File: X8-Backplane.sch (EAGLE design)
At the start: 17 parts, among them IC1 MAX3467CPA, U1 LM2678

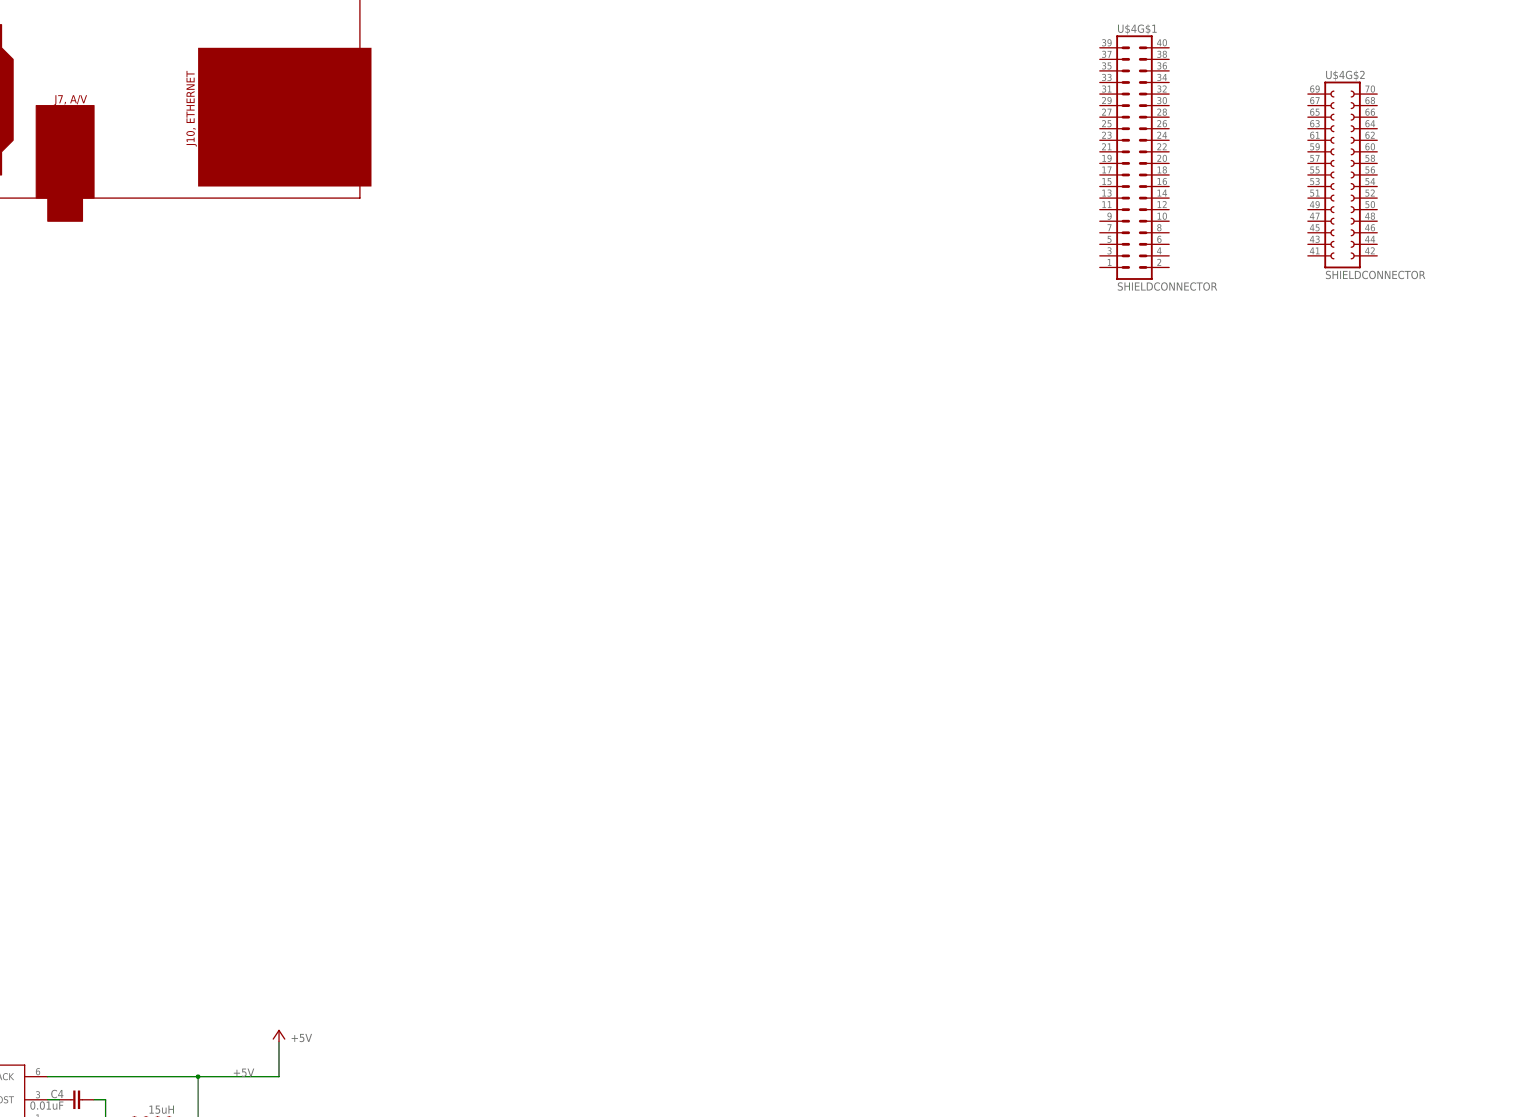
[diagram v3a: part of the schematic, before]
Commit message: Mostly routed
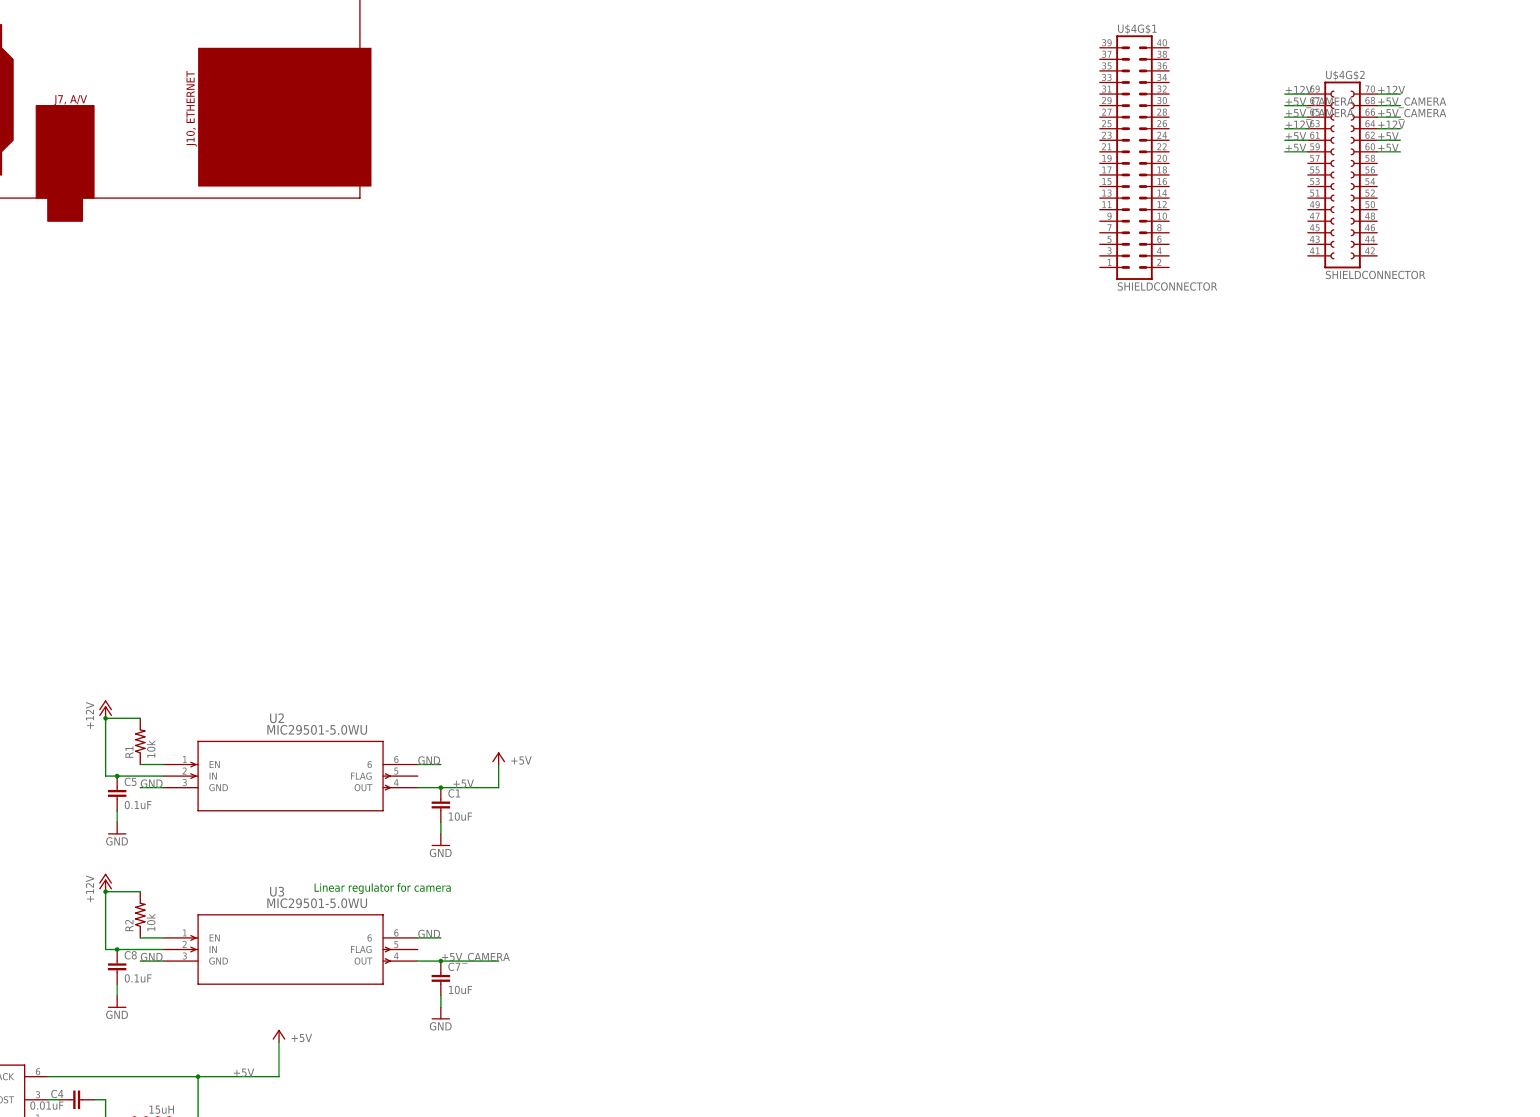
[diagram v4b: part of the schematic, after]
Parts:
- added C1, C7: 10uF, SparkFun-Passives:CAP0603-CAP
- added C5, C8: 0.1uF, SparkFun-Passives:CAP0603-CAP
- added R1, R2: 10k, SparkFun-Passives:RESISTOR0603-RES
- added U2, U3: MIC29501-5.0WU, LDO:MIC29501-5.0WU
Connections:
- new net +5V_CAMERA: C7.1, U$4G$2.25, U$4G$2.26, U$4G$2.27, U$4G$2.28, U3.OUT
- new net EN1: R1.1, U2.EN
- new net EN2: R2.1, U3.EN
- net +12V: now also C5.1, C8.1, R1.2, R2.2, U$4G$2.23, U$4G$2.24, U$4G$2.29, U$4G$2.30, U2.IN, U3.IN
- net +5V: now also C1.1, U$4G$2.19, U$4G$2.20, U$4G$2.21, U$4G$2.22, U2.OUT
- net GND: now also C1.2, C5.2, C7.2, C8.2, U2.6, U2.GND, U3.6, U3.GND
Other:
- note added: "Linear regulator for camera"
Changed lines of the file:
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@@
 <part name="GND1" library="supply1" deviceset="GND" device=""/>
 <part name="U$7" library="test_lib" deviceset="PCA9615" device=""/>
+<part name="U2" library="LDO" deviceset="MIC29501-5.0WU" device=""/>
+<part name="U3" library="LDO" deviceset="MIC29501-5.0WU" device=""/>
+<part name="P+1" library="supply1" deviceset="+12V" device=""/>
+<part name="P+3" library="supply1" deviceset="+12V" device=""/>
+<part name="R1" library="SparkFun-Passives" deviceset="RESISTOR" device="0603-RES" value="10k"/>
+<part name="R2" library="SparkFun-Passives" deviceset="RESISTOR" device="0603-RES" value="10k"/>
+<part name="P+5" library="supply1" deviceset="+5V" device=""/>
+<part name="C1" library="SparkFun-Passives" deviceset="CAP" device="0603-CAP" value="10uF"/>
+<part name="C5" library="SparkFun-Passives" deviceset="CAP" device="0603-CAP" value="0.1uF"/>
+<part name="C7" library="SparkFun-Passives" deviceset="CAP" device="0603-CAP" value="10uF"/>
+<part name="C8" library="SparkFun-Passives" deviceset="CAP" device="0603-CAP" value="0.1uF"/>
+<part name="GND2" library="SparkFun-Aesthetics" deviceset="GND" device=""/>
+<part name="GND3" library="SparkFun-Aesthetics" deviceset="GND" device=""/>
+<part name="GND4" library="SparkFun-Aesthetics" deviceset="GND" device=""/>
+<part name="GND7" library="SparkFun-Aesthetics" deviceset="GND" device=""/>
 </parts>
 <sheets>
 <sheet>
 <plain>
+<text x="193.04" y="-68.58" size="1.778" layer="91">Linear regulator for camera</text>
 </plain>
 <instances>
@@
 <instance part="GND1" gate="1" x="513.08" y="153.67"/>
 <instance part="U$7" gate="G$1" x="408.94" y="165.1"/>
+<instance part="U2" gate="A" x="160.02" y="-40.64"/>
+<instance part="U3" gate="A" x="160.02" y="-78.74"/>
+<instance part="P+1" gate="1" x="147.32" y="-27.94"/>
+<instance part="P+3" gate="1" x="147.32" y="-66.04"/>
+<instance part="R1" gate="G$1" x="154.94" y="-35.56" rot="R90"/>
+<instance part="R2" gate="G$1" x="154.94" y="-73.66" rot="R90"/>
+<instance part="P+5" gate="1" x="233.68" y="-38.1" smashed="yes">
+<attribute name="VALUE" x="236.22" y="-40.64" size="1.778" layer="96"/>
+</instance>
+<instance part="C1" gate="G$1" x="220.98" y="-50.8"/>
+<instance part="C5" gate="G$1" x="149.86" y="-48.26"/>
+<instance part="C7" gate="G$1" x="220.98" y="-88.9"/>
+<instance part="C8" gate="G$1" x="149.86" y="-86.36"/>
+<instance part="GND2" gate="1" x="149.86" y="-55.88"/>
+<instance part="GND3" gate="1" x="220.98" y="-96.52"/>
+<instance part="GND4" gate="1" x="220.98" y="-58.42"/>
+<instance part="GND7" gate="1" x="149.86" y="-93.98"/>
 </instances>
 <busses>
@@
 <pinref part="GND1" gate="1" pin="GND"/>
 </segment>
+<segment>
+<pinref part="U2" gate="A" pin="GND"/>
+<wire x1="160.02" y1="-45.72" x2="154.94" y2="-45.72" width="0.1524" layer="91"/>
+<label x="154.94" y="-45.72" size="1.778" layer="95"/>
+</segment>
+<segment>
+<pinref part="U3" gate="A" pin="GND"/>
+<wire x1="160.02" y1="-83.82" x2="154.94" y2="-83.82" width="0.1524" layer="91"/>
+<label x="154.94" y="-83.82" size="1.778" layer="95"/>
+</segment>
+<segment>
+<pinref part="U2" gate="A" pin="6"/>
+<wire x1="215.9" y1="-40.64" x2="220.98" y2="-40.64" width="0.1524" layer="91"/>
+<label x="215.9" y="-40.64" size="1.778" layer="95"/>
+</segment>
+<segment>
+<pinref part="U3" gate="A" pin="6"/>
+<wire x1="215.9" y1="-78.74" x2="220.98" y2="-78.74" width="0.1524" layer="91"/>
+<label x="215.9" y="-78.74" size="1.778" layer="95"/>
+</segment>
+<segment>
+<pinref part="C5" gate="G$1" pin="2"/>
+<wire x1="149.86" y1="-50.8" x2="149.86" y2="-53.34" width="0.1524" layer="91"/>
+<pinref part="GND2" gate="1" pin="GND"/>
+</segment>
+<segment>
+<pinref part="C1" gate="G$1" pin="2"/>
+<wire x1="220.98" y1="-53.34" x2="220.98" y2="-55.88" width="0.1524" layer="91"/>
+<pinref part="GND4" gate="1" pin="GND"/>
+</segment>
+<segment>
+<pinref part="C8" gate="G$1" pin="2"/>
+<wire x1="149.86" y1="-88.9" x2="149.86" y2="-91.44" width="0.1524" layer="91"/>
+<pinref part="GND7" gate="1" pin="GND"/>
+</segment>
+<segment>
+<pinref part="C7" gate="G$1" pin="2"/>
+<wire x1="220.98" y1="-91.44" x2="220.98" y2="-93.98" width="0.1524" layer="91"/>
+<pinref part="GND3" gate="1" pin="GND"/>
+</segment>
 </net>
 <net name="+12V" class="0">
@@
 <junction x="68.58" y="-119.38"/>
 </segment>
+<segment>
+<pinref part="P+1" gate="1" pin="+12V"/>
+<pinref part="R1" gate="G$1" pin="2"/>
+<wire x1="147.32" y1="-30.48" x2="154.94" y2="-30.48" width="0.1524" layer="91"/>
+<pinref part="U2" gate="A" pin="IN"/>
+<wire x1="147.32" y1="-30.48" x2="147.32" y2="-43.18" width="0.1524" layer="91"/>
+<wire x1="147.32" y1="-43.18" x2="149.86" y2="-43.18" width="0.1524" layer="91"/>
+<junction x="147.32" y="-30.48"/>
+<pinref part="C5" gate="G$1" pin="1"/>
+<wire x1="149.86" y1="-43.18" x2="160.02" y2="-43.18" width="0.1524" layer="91"/>
+<junction x="149.86" y="-43.18"/>
+</segment>
+<segment>
+<pinref part="P+3" gate="1" pin="+12V"/>
+<pinref part="R2" gate="G$1" pin="2"/>
+<wire x1="147.32" y1="-68.58" x2="154.94" y2="-68.58" width="0.1524" layer="91"/>
+<pinref part="U3" gate="A" pin="IN"/>
+<wire x1="147.32" y1="-68.58" x2="147.32" y2="-81.28" width="0.1524" layer="91"/>
+<wire x1="147.32" y1="-81.28" x2="149.86" y2="-81.28" width="0.1524" layer="91"/>
+<junction x="147.32" y="-68.58"/>
+<pinref part="C8" gate="G$1" pin="1"/>
+<wire x1="149.86" y1="-81.28" x2="160.02" y2="-81.28" width="0.1524" layer="91"/>
+<junction x="149.86" y="-81.28"/>
+</segment>
+<segment>
+<pinref part="U$4" gate="G$2" pin="29"/>
+<wire x1="411.48" y1="106.68" x2="406.4" y2="106.68" width="0.1524" layer="91"/>
+<label x="406.4" y="106.68" size="1.778" layer="95"/>
+</segment>
+<segment>
+<pinref part="U$4" gate="G$2" pin="30"/>
+<wire x1="426.72" y1="106.68" x2="431.8" y2="106.68" width="0.1524" layer="91"/>
+<label x="426.72" y="106.68" size="1.778" layer="95"/>
+</segment>
+<segment>
+<pinref part="U$4" gate="G$2" pin="23"/>
+<wire x1="411.48" y1="99.06" x2="406.4" y2="99.06" width="0.1524" layer="91"/>
+<label x="406.4" y="99.06" size="1.778" layer="95"/>
+</segment>
+<segment>
+<pinref part="U$4" gate="G$2" pin="24"/>
+<wire x1="426.72" y1="99.06" x2="431.8" y2="99.06" width="0.1524" layer="91"/>
+<label x="426.72" y="99.06" size="1.778" layer="95"/>
+</segment>
 </net>
 <net name="+5V" class="0">
@@
 <junction x="177.8" y="-119.38"/>
 </segment>
+<segment>
+<pinref part="U2" gate="A" pin="OUT"/>
+<pinref part="P+5" gate="1" pin="+5V"/>
+<wire x1="215.9" y1="-45.72" x2="220.98" y2="-45.72" width="0.1524" layer="91"/>
+<wire x1="220.98" y1="-45.72" x2="233.68" y2="-45.72" width="0.1524" layer="91"/>
+<wire x1="233.68" y1="-45.72" x2="233.68" y2="-40.64" width="0.1524" layer="91"/>
+<label x="223.52" y="-45.72" size="1.778" layer="95"/>
+<pinref part="C1" gate="G$1" pin="1"/>
+<junction x="220.98" y="-45.72"/>
+</segment>
+<segment>
+<pinref part="U$4" gate="G$2" pin="21"/>
+<wire x1="411.48" y1="96.52" x2="406.4" y2="96.52" width="0.1524" layer="91"/>
+<label x="406.4" y="96.52" size="1.778" layer="95"/>
+</segment>
+<segment>
+<pinref part="U$4" gate="G$2" pin="19"/>
+<wire x1="411.48" y1="93.98" x2="406.4" y2="93.98" width="0.1524" layer="91"/>
+<label x="406.4" y="93.98" size="1.778" layer="95"/>
+</segment>
+<segment>
+<pinref part="U$4" gate="G$2" pin="22"/>
+<wire x1="426.72" y1="96.52" x2="431.8" y2="96.52" width="0.1524" layer="91"/>
+<label x="426.72" y="96.52" size="1.778" layer="95"/>
+</segment>
+<segment>
+<pinref part="U$4" gate="G$2" pin="20"/>
+<wire x1="426.72" y1="93.98" x2="431.8" y2="93.98" width="0.1524" layer="91"/>
+<label x="426.72" y="93.98" size="1.778" layer="95"/>
+</segment>
 </net>
 <net name="N$4" class="0">
@@
 </segment>
 </net>
+<net name="EN1" class="0">
+<segment>
+<pinref part="R1" gate="G$1" pin="1"/>
+<pinref part="U2" gate="A" pin="EN"/>
+<wire x1="154.94" y1="-40.64" x2="160.02" y2="-40.64" width="0.1524" layer="91"/>
+</segment>
+</net>
+<net name="EN2" class="0">
+<segment>
+<pinref part="R2" gate="G$1" pin="1"/>
+<pinref part="U3" gate="A" pin="EN"/>
+<wire x1="154.94" y1="-78.74" x2="160.02" y2="-78.74" width="0.1524" layer="91"/>
+</segment>
+</net>
+<net name="+5V_CAMERA" class="0">
+<segment>
+<pinref part="U3" gate="A" pin="OUT"/>
+<wire x1="233.68" y1="-83.82" x2="220.98" y2="-83.82" width="0.1524" layer="91"/>
+<label x="220.98" y="-83.82" size="1.778" layer="95"/>
+<pinref part="C7" gate="G$1" pin="1"/>
+<wire x1="220.98" y1="-83.82" x2="215.9" y2="-83.82" width="0.1524" layer="91"/>
+<junction x="220.98" y="-83.82"/>
+</segment>
+<segment>
+<pinref part="U$4" gate="G$2" pin="27"/>
+<wire x1="411.48" y1="104.14" x2="406.4" y2="104.14" width="0.1524" layer="91"/>
+<label x="406.4" y="104.14" size="1.778" layer="95"/>
+</segment>
+<segment>
+<pinref part="U$4" gate="G$2" pin="25"/>
+<wire x1="411.48" y1="101.6" x2="406.4" y2="101.6" width="0.1524" layer="91"/>
+<label x="406.4" y="101.6" size="1.778" layer="95"/>
+</segment>
+<segment>
+<pinref part="U$4" gate="G$2" pin="28"/>
+<wire x1="426.72" y1="104.14" x2="431.8" y2="104.14" width="0.1524" layer="91"/>
+<label x="426.72" y="104.14" size="1.778" layer="95"/>
+</segment>
+<segment>
+<pinref part="U$4" gate="G$2" pin="26"/>
+<wire x1="426.72" y1="101.6" x2="431.8" y2="101.6" width="0.1524" layer="91"/>
+<label x="426.72" y="101.6" size="1.778" layer="95"/>
+</segment>
+</net>

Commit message: removed buck regulator circuit
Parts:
- removed C10, C6, C9: 150uF, PowerComponents:C-TANTALUM(10UF_150UF)
- removed C11, C12, C13, C2: 10uF, PowerComponents:C-TANTALUM(10UF_150UF)
- removed C3: 0.47uF, SparkFun-Capacitors:CAP0805
- removed C4: 0.01uF, SparkFun-Passives:CAP0603-CAP
- removed U$1: SWITCHMODE_SCHOTTKY, PowerComponents:SWITCHMODE_SCHOTTKY
- removed U$2: 15uH, DiscreteComponents:HCMA1305
- removed U1: LM2678, PowerComponents:LM2678
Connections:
- net +5V_CAMERA renamed +5V_CAMERA_TUBE
- removed net N$2: C4.1, U1.BOOST
- removed net N$3: C4.2, U$1.P$4, U$2.1, U1.OUTPUT
- net +12V: no longer C11.+, C12.+, C13.+, C2.+, C3.1, U1.VIN
- net +5V: no longer C10.+, C6.+, C9.+, U$2.2, U1.FEEDBACK
- net GND: no longer C10.-, C11.-, C12.-, C13.-, C2.-, C3.2, C6.-, C9.-, U$1.P$1, U$1.P$3, U1.GND, U1.TABGND

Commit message: added some new parts
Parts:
- added U$1: MAX3491, BackplaneParts:MAX3491
- added U$2: BD6221, HBridge:BD6221
- added U1: BD6221FSOP, CamSensComponents:BD6221FSOP
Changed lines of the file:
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@@
 <part name="GND4" library="SparkFun-Aesthetics" deviceset="GND" device=""/>
 <part name="GND7" library="SparkFun-Aesthetics" deviceset="GND" device=""/>
+<part name="U$1" library="BackplaneParts" deviceset="MAX3491" device=""/>
+<part name="U1" library="CamSensComponents" deviceset="BD6221F" device="SOP"/>
+<part name="U$2" library="HBridge" deviceset="BD6221" device=""/>
 </parts>
 <sheets>
@@
 <instance part="GND4" gate="1" x="220.98" y="-58.42"/>
 <instance part="GND7" gate="1" x="149.86" y="-93.98"/>
+<instance part="U$1" gate="G$1" x="495.3" y="106.68"/>
+<instance part="U1" gate="U1" x="500.38" y="66.04"/>
+<instance part="U$2" gate="G$1" x="533.4" y="66.04" rot="R90"/>
 </instances>
 <busses>

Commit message: finished adding components, added descriptions of pins
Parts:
- removed IC1: MAX3467CPA, maxim:MAX3467CPA
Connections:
- removed net +3V3: IC1.VCC
- removed net COM_A: IC1.A
- removed net COM_B: IC1.B
- removed net COM_Y: IC1.Y
- removed net COM_Z: IC1.Z
- removed net TETHER_RX: IC1.RO
- removed net TETHER_TX: IC1.DI
- net GND: no longer IC1.GND
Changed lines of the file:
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@@
 <part name="U$3" library="Other" deviceset="BNO055_9DOF_BREAKOUT" device=""/>
 <part name="U$4" library="backplane_to_shield_connector" deviceset="SHIELDCONNECTOR" device=""/>
-<part name="IC1" library="maxim" deviceset="MAX3467*" device="PA" technology="C"/>
-<part name="+3V1" library="supply1" deviceset="+3V3" device=""/>
-<part name="GND1" library="supply1" deviceset="GND" device=""/>
 <part name="U$7" library="test_lib" deviceset="PCA9615" device=""/>
 <part name="U2" library="LDO" deviceset="MIC29501-5.0WU" device=""/>
@@
 <instance part="U$4" gate="G$1" x="373.38" y="91.44"/>
 <instance part="U$4" gate="G$2" x="419.1" y="88.9"/>
-<instance part="IC1" gate="G$1" x="496.57" y="172.72"/>
-<instance part="+3V1" gate="G$1" x="513.08" y="191.77"/>
-<instance part="GND1" gate="1" x="513.08" y="153.67"/>
 <instance part="U$7" gate="G$1" x="408.94" y="165.1"/>
 <instance part="U2" gate="A" x="160.02" y="-40.64"/>
@@
 <nets>
 <net name="GND" class="0">
-<segment>
-<pinref part="IC1" gate="G$1" pin="GND"/>
-<wire x1="509.27" y1="160.02" x2="513.08" y2="160.02" width="0.1524" layer="91"/>
-<wire x1="513.08" y1="160.02" x2="513.08" y2="156.21" width="0.1524" layer="91"/>
-<pinref part="GND1" gate="1" pin="GND"/>
-</segment>
 <segment>
 <pinref part="U2" gate="A" pin="GND"/>
@@
 </segment>
 </net>
-<net name="+3V3" class="0">
-<segment>
-<pinref part="IC1" gate="G$1" pin="VCC"/>
-<wire x1="509.27" y1="185.42" x2="513.08" y2="185.42" width="0.1524" layer="91"/>
-<wire x1="513.08" y1="185.42" x2="513.08" y2="189.23" width="0.1524" layer="91"/>
-<pinref part="+3V1" gate="G$1" pin="+3V3"/>
-</segment>
-</net>
-<net name="TETHER_RX" class="0">
-<segment>
-<pinref part="IC1" gate="G$1" pin="RO"/>
-<wire x1="486.41" y1="167.64" x2="485.14" y2="167.64" width="0.1524" layer="91"/>
-<label x="485.14" y="167.64" size="1.27" layer="95" rot="R180" xref="yes"/>
-</segment>
-</net>
-<net name="TETHER_TX" class="0">
-<segment>
-<label x="485.14" y="177.8" size="1.27" layer="95" rot="R180" xref="yes"/>
-<pinref part="IC1" gate="G$1" pin="DI"/>
-<wire x1="485.14" y1="177.8" x2="486.41" y2="177.8" width="0.1524" layer="91"/>
-</segment>
-</net>
-<net name="COM_A" class="0">
-<segment>
-<pinref part="IC1" gate="G$1" pin="A"/>
-<wire x1="509.27" y1="170.18" x2="513.08" y2="170.18" width="0.1524" layer="91"/>
-<label x="513.08" y="170.18" size="1.27" layer="95" xref="yes"/>
-</segment>
-</net>
-<net name="COM_B" class="0">
-<segment>
-<pinref part="IC1" gate="G$1" pin="B"/>
-<wire x1="509.27" y1="165.1" x2="513.08" y2="165.1" width="0.1524" layer="91"/>
-<label x="513.08" y="165.1" size="1.27" layer="95" xref="yes"/>
-</segment>
-</net>
-<net name="COM_Y" class="0">
-<segment>
-<pinref part="IC1" gate="G$1" pin="Y"/>
-<wire x1="509.27" y1="180.34" x2="513.08" y2="180.34" width="0.1524" layer="91"/>
-<label x="513.08" y="180.34" size="1.27" layer="95" xref="yes"/>
-</segment>
-</net>
-<net name="COM_Z" class="0">
-<segment>
-<pinref part="IC1" gate="G$1" pin="Z"/>
-<wire x1="509.27" y1="175.26" x2="513.08" y2="175.26" width="0.1524" layer="91"/>
-<label x="513.08" y="175.26" size="1.27" layer="95" xref="yes"/>
-</segment>
-</net>
